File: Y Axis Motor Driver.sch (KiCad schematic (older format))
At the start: 35 parts, among them J1 Motor Y, U1 TMC2209-LA

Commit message: Dodano brakujący footprint dla R1
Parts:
- R1: footprint (none) -> Resistor_SMD:R_0603_1608Metric
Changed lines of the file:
@@
 F 0 "R1" V 1593 1250 50  0000 C CNN
 F 1 "0Ω" V 1684 1250 50  0000 C CNN
-F 2 "" V 1730 1250 50  0001 C CNN
+F 2 "Resistor_SMD:R_0603_1608Metric" V 1730 1250 50  0001 C CNN
 F 3 "~" H 1800 1250 50  0001 C CNN
 	1    1800 1250

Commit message: Routing emergnency, photo barier, relay, voltage detect, analog, footprint improvment
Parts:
- U1: footprint footprints:TMC2209-LA -> footprints:QFN-28_5X5_3X8_EPAD
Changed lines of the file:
@@
 F 0 "U1" H 2850 4850 60  0000 L CNN
 F 1 "TMC2209-LA" H 2850 4750 60  0000 L CNN
-F 2 "footprints:TMC2209-LA" V 3700 3750 60  0001 C CNN
+F 2 "footprints:QFN-28_5X5_3X8_EPAD" V 3700 3750 60  0001 C CNN
 F 3 "https://www.trinamic.com/fileadmin/assets/Products/ICs_Documents/TMC2209_Datasheet_V103.pdf" H 2700 4400 60  0001 C CNN
 F 4 "10.30" H 3750 3750 50  0001 C CNN "Cena"

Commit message: Start TMC routing
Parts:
- removed TP1: Z_OB2, TestPoint:TestPoint_Pad_D1.5mm, symbol Connector:TestPoint
- removed TP2: Z_OB1, TestPoint:TestPoint_Pad_D1.5mm, symbol Connector:TestPoint
- removed TP3: Z_OA2, TestPoint:TestPoint_Pad_D1.5mm, symbol Connector:TestPoint
- removed TP4: Z_OA1, TestPoint:TestPoint_Pad_D1.5mm, symbol Connector:TestPoint
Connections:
- net at U1.1 (OB2): now also FB1.2; no longer FB4.2
- net at U1.21 (OA2): now also FB4.2; no longer FB2.2
- net at U1.24 (OA1): now also FB3.2; no longer FB1.2
- net at U1.26 (OB1): now also FB2.2; no longer FB3.2
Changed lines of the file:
@@
 	0    1    1    0
 $EndComp
-Wire Wire Line
-	4600 3700 6250 3700
-Wire Wire Line
-	6250 3700 6250 3200
-Wire Wire Line
-	4600 3600 6150 3600
-Wire Wire Line
-	6150 3600 6150 3050
 $Comp
 L Device:C_Small C?
@@
 $EndComp
 Wire Wire Line
-	9400 3050 9400 3450
-Wire Wire Line
-	9050 3200 9050 3450
-Wire Wire Line
 	8350 3900 8350 4250
 Connection ~ 8700 3750
@@
 Text Notes 10350 3000 0    50   ~ 0
 Złącze JST XH2.5
-Wire Wire Line
-	8350 3900 8350 3450
-$Comp
-L Connector:TestPoint TP?
-U 1 1 5E249152
-P 8350 3450
-AR Path="/5DE588DC/5E249152" Ref="TP?"  Part="1"
-AR Path="/5DE587B9/5E249152" Ref="TP1"  Part="1"
-F 0 "TP1" V 8250 3500 50  0000 L CNN
-F 1 "Z_OB2" V 8450 3500 50  0000 L CNN
-F 2 "TestPoint:TestPoint_Pad_D1.5mm" H 8550 3450 50  0001 C CNN
-F 3 "~" H 8550 3450 50  0001 C CNN
-	1    8350 3450
-	0    1    1    0
-$EndComp
-$Comp
-L Connector:TestPoint TP?
-U 1 1 5E24915B
-P 8700 3450
-AR Path="/5DE588DC/5E24915B" Ref="TP?"  Part="1"
-AR Path="/5DE587B9/5E24915B" Ref="TP2"  Part="1"
-F 0 "TP2" V 8600 3500 50  0000 L CNN
-F 1 "Z_OB1" V 8800 3500 50  0000 L CNN
-F 2 "TestPoint:TestPoint_Pad_D1.5mm" H 8900 3450 50  0001 C CNN
-F 3 "~" H 8900 3450 50  0001 C CNN
-	1    8700 3450
-	0    1    1    0
-$EndComp
-Wire Wire Line
-	8700 3450 8700 3750
-$Comp
-L Connector:TestPoint TP?
-U 1 1 5E249163
-P 9050 3450
-AR Path="/5DE588DC/5E249163" Ref="TP?"  Part="1"
-AR Path="/5DE587B9/5E249163" Ref="TP3"  Part="1"
-F 0 "TP3" V 8950 3500 50  0000 L CNN
-F 1 "Z_OA2" V 9150 3500 50  0000 L CNN
-F 2 "TestPoint:TestPoint_Pad_D1.5mm" H 9250 3450 50  0001 C CNN
-F 3 "~" H 9250 3450 50  0001 C CNN
-	1    9050 3450
-	0    1    1    0
-$EndComp
-$Comp
-L Connector:TestPoint TP?
-U 1 1 5E24916B
-P 9400 3450
-AR Path="/5DE588DC/5E24916B" Ref="TP?"  Part="1"
-AR Path="/5DE587B9/5E24916B" Ref="TP4"  Part="1"
-F 0 "TP4" V 9300 3500 50  0000 L CNN
-F 1 "Z_OA1" V 9500 3500 50  0000 L CNN
-F 2 "TestPoint:TestPoint_Pad_D1.5mm" H 9600 3450 50  0001 C CNN
-F 3 "~" H 9600 3450 50  0001 C CNN
-	1    9400 3450
-	0    1    1    0
-$EndComp
 Text GLabel 1600 3000 0    50   Input ~ 0
 Y_STEP
@@
 	2900 3100 1600 3100
 Wire Wire Line
-	6350 3800 6350 3750
-Wire Wire Line
-	4600 3800 6350 3800
-Wire Wire Line
 	7250 3050 7500 3050
 Wire Wire Line
@@
 Wire Wire Line
 	7900 3200 9050 3200
-Wire Wire Line
-	6350 3750 7050 3750
-Wire Wire Line
-	4600 3900 7050 3900
 Wire Wire Line
 	6250 3200 7050 3200
@@
 	0    1    1    0
 $EndComp
-Connection ~ 9400 3450
-Connection ~ 9050 3450
 Wire Wire Line
 	7900 3750 8700 3750
@@
 	0    1    1    0
 $EndComp
-Wire Wire Line
-	9400 3450 9400 4250
 $Comp
 L Device:D_TVS_ALT D3
@@
 	8250 4200 9700 4200
 Wire Wire Line
-	9050 3450 9050 4250
-Wire Wire Line
 	9400 4550 9400 5150
 $Comp
@@
 Wire Wire Line
 	9750 3750 9850 3750
+Wire Wire Line
+	6450 3750 7050 3750
+Wire Wire Line
+	4600 3900 6150 3900
+Wire Wire Line
+	6150 3050 6150 3900
+Wire Wire Line
+	6250 3800 4600 3800
+Wire Wire Line
+	6250 3200 6250 3800
+Wire Wire Line
+	4600 3600 6450 3600
+Wire Wire Line
+	6450 3600 6450 3750
+Wire Wire Line
+	7050 3900 6350 3900
+Wire Wire Line
+	6350 3900 6350 3700
+Wire Wire Line
+	6350 3700 4600 3700
+Wire Wire Line
+	9050 3200 9050 4250
+Wire Wire Line
+	9400 3050 9400 4250
 $EndSCHEMATC

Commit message: TMC2209 routing step 2/3
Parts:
- removed C1: 330uF, Capacitor_THT:CP_Radial_D10.0mm_P5.00mm, symbol Device:CP_Small
- removed C2: 10uF, Capacitor_SMD:C_1210_3225Metric, symbol Device:C_Small
- removed C3: 1uF, Capacitor_SMD:C_0805_2012Metric, symbol Device:C_Small
- added C2, C3: 120uF, Capacitor_THT:CP_Radial_D8.0mm_P3.50mm, symbol Device:CP_Small
- added C87: 10uF, Capacitor_SMD:C_1210_3225Metric, symbol Device:C_Small
- added C88: 1uF, Capacitor_SMD:C_0805_2012Metric, symbol Device:C_Small
- added C89: 0.1uF, Capacitor_SMD:C_0603_1608Metric, symbol Device:C_Small
- C4: value 0.1uF -> 10uF; footprint Capacitor_SMD:C_0603_1608Metric -> Capacitor_SMD:C_1210_3225Metric; Cena 0.05982 -> 1.45250; Model CL10B104KB8NNNC -> CL32B106KBJNNNE
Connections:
- net GND: now also C2.2, C3.2, C87.2, C88.2, C89.2; no longer R3.1
- net VCC: now also R3.1
- net VS: now also C2.1, C3.1, C87.1, C88.1, C89.1

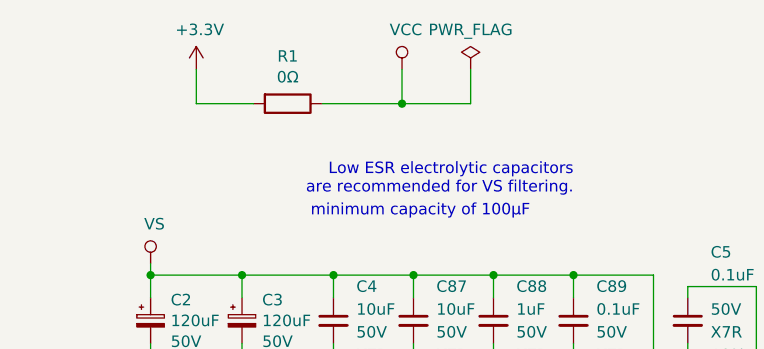
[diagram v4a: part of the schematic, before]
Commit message: Test points, start power plane routing, little change on schematic
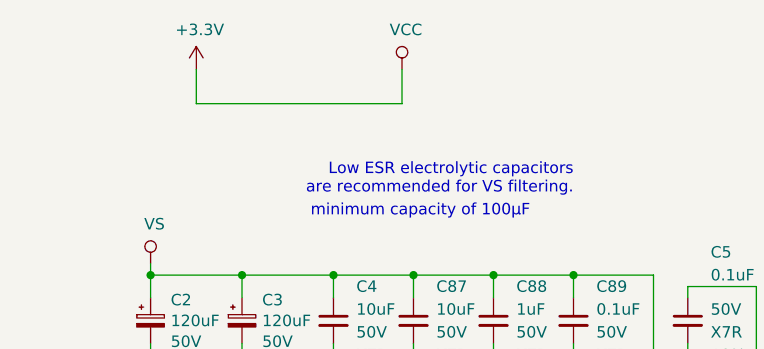
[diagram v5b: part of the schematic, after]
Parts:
- removed R1: 0Ω, Resistor_SMD:R_0603_1608Metric, symbol Device:R
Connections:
- net VCC is gone; now on net +3V3: C6.1, R3.1, U1.15 (VCC_IO), U1.9 (MS1/AD0)
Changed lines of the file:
@@
 	1400 1100 1400 1250
-Wire Wire Line
-	1400 1250 1650 1250
-Wire Wire Line
-	1950 1250 2300 1250
 Wire Wire Line
 	2300 1250 2300 1100
@@
 $EndComp
 $Comp
-L Device:R R?
-U 1 1 5E2371E0
-P 1800 1250
-AR Path="/5DFB2EC0/5E2371E0" Ref="R?"  Part="1"
-AR Path="/5DE587B9/5E2371E0" Ref="R1"  Part="1"
-F 0 "R1" V 1593 1250 50  0000 C CNN
-F 1 "0Ω" V 1684 1250 50  0000 C CNN
-F 2 "Resistor_SMD:R_0603_1608Metric" V 1730 1250 50  0001 C CNN
-F 3 "~" H 1800 1250 50  0001 C CNN
-	1    1800 1250
-	0    1    1    0
-$EndComp
-$Comp
 L Device:D_TVS_ALT D1
 U 1 1 5E251EB1
@@
 Wire Wire Line
 	2200 4800 2200 4850
-$Comp
-L power:PWR_FLAG #FLG0101
-U 1 1 5E3F672C
-P 2600 1100
-F 0 "#FLG0101" H 2600 1175 50  0001 C CNN
-F 1 "PWR_FLAG" H 2600 1273 50  0000 C CNN
-F 2 "" H 2600 1100 50  0001 C CNN
-F 3 "~" H 2600 1100 50  0001 C CNN
-	1    2600 1100
-	1    0    0    -1
-$EndComp
-Wire Wire Line
-	2300 1250 2600 1250
-Wire Wire Line
-	2600 1250 2600 1100
-Connection ~ 2300 1250
+Wire Wire Line
+	1400 1250 2300 1250
 $EndSCHEMATC

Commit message: Added 3d packages, improved TMC2209 footprint
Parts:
- U1: footprint footprints:QFN-28_5X5_3X8_EPAD -> footprints:QFN-28_5X5mm_P0.5mm_EP3.35x.3.35mm
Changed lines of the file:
@@
 F 0 "U1" H 2850 4850 60  0000 L CNN
 F 1 "TMC2209-LA" H 2850 4750 60  0000 L CNN
-F 2 "footprints:QFN-28_5X5_3X8_EPAD" V 3700 3750 60  0001 C CNN
+F 2 "footprints:QFN-28_5X5mm_P0.5mm_EP3.35x.3.35mm" V 3700 3750 60  0001 C CNN
 F 3 "https://www.trinamic.com/fileadmin/assets/Products/ICs_Documents/TMC2209_Datasheet_V103.pdf" H 2700 4400 60  0001 C CNN
 F 4 "10.30" H 3750 3750 50  0001 C CNN "Cena"

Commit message: Updated BOM on schematics
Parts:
- C10, C5, C6, C8, C89: Cena 0.05982 -> 0.07894; Link (none) -> https://www.tme.eu/pl/details/cl10b104kb8nnnc/kondensatory-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; Model CL10B104KB8NNNC -> CL10B104KB8NNNC; Opis (none) -> Kondensator: ceramiczny; MLCC; 100nF; 50V; X7R; ±10%; SMD; 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
- C11, C12, C13, C14: Opis (none) -> Kondensator: ceramiczny; MLCC; 470pF; 100VDC; C0G; ±5%; SMD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
- C4, C87: Link (none) -> https://www.tme.eu/pl/details/cl32b106kbjnnne/kondensatory-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; Opis (none) -> Kondensator: ceramiczny; MLCC; 10uF; 50V; X7R; ±10%; SMD; 1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
- C7: Opis (none) -> Kondensator: ceramiczny; MLCC; 22nF; 50V; X7R; ±10%; SMD; 0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
- C88: Link (none) -> https://www.tme.eu/pl/details/cl21b105kbfnnng/kondensatory-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; Opis (none) -> Kondensator: ceramiczny; MLCC; 1uF; 50V; X7R; ±10%; SMD; 08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
- C9: Opis (none) -> Kondensator: ceramiczny; MLCC; 2,2uF; 10V; X5R; ±10%; SMD; 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
- R3: Link (none) -> https://www.tme.eu/pl/details/smd0603-100k-1%25/rezystory-s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; Model (none) -> 0603SAF1003T5E; Opis (none) -> Rezystor: thick film; SMD; 0603; 100kΩ; 0,1W; ±1%; -55÷155°C; Producent (none) -> ROYAL OHM
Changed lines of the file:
@@
 F 10 "10%" H 5050 3200 50  0001 C CNN "Tolerancja"
 F 11 "SMD" H 5050 3200 50  0001 C CNN "Typ"
+F 12 "Kondensator: ceramiczny; MLCC; 22nF; 50V; X7R; ±10%; SMD; 0603" H 5050 3200 50  0001 C CNN "Opis"
 	1    5050 3200
 	1    0    0    -1
@@
 F 5 "X7R" H 3650 2150 50  0000 L CNN "Dielektryk"
 F 6 "10%" H 3650 2050 50  0000 L CNN "Tolerancja"
-F 7 "CL10B104KB8NNNC " H 3550 2200 50  0001 C CNN "Model"
-F 8 "0.05982" H 3550 2200 50  0001 C CNN "Cena"
+F 7 "CL10B104KB8NNNC" H 3550 2200 50  0001 C CNN "Model"
+F 8 "0.07894" H 3550 2200 50  0001 C CNN "Cena"
 F 9 "SAMSUNG" H 3550 2200 50  0001 C CNN "Producent"
 F 10 "SMD" H 3550 2200 50  0001 C CNN "Typ"
+F 11 "https://www.tme.eu/pl/details/cl10b104kb8nnnc/kondensatory-mlcc-smd-0603/samsung/" H 3550 2200 50  0001 C CNN "Link"
+F 12 "Kondensator: ceramiczny; MLCC; 100nF; 50V; X7R; ±10%; SMD; 0603" H 3550 2200 50  0001 C CNN "Opis"
 	1    3550 2200
 	1    0    0    -1
@@
 F 5 "X7R" H 4250 2150 50  0000 L CNN "Dielektryk"
 F 6 "10%" H 4250 2050 50  0000 L CNN "Tolerancja"
-F 7 "CL10B104KB8NNNC " H 4150 2200 50  0001 C CNN "Model"
-F 8 "0.05982" H 4150 2200 50  0001 C CNN "Cena"
+F 7 "CL10B104KB8NNNC" H 4150 2200 50  0001 C CNN "Model"
+F 8 "0.07894" H 4150 2200 50  0001 C CNN "Cena"
 F 9 "SAMSUNG" H 4150 2200 50  0001 C CNN "Producent"
 F 10 "SMD" H 4150 2200 50  0001 C CNN "Typ"
+F 11 "https://www.tme.eu/pl/details/cl10b104kb8nnnc/kondensatory-mlcc-smd-0603/samsung/" H 4150 2200 50  0001 C CNN "Link"
+F 12 "Kondensator: ceramiczny; MLCC; 100nF; 50V; X7R; ±10%; SMD; 0603" H 4150 2200 50  0001 C CNN "Opis"
 	1    4150 2200
 	1    0    0    -1
@@
 F 5 "X7R" H 5492 4359 50  0000 L CNN "Dielektryk"
 F 6 "10%" H 5492 4268 50  0000 L CNN "Tolerancja"
-F 7 "CL10B104KB8NNNC " H 5400 4450 50  0001 C CNN "Model"
-F 8 "0.05982" H 5400 4450 50  0001 C CNN "Cena"
+F 7 "CL10B104KB8NNNC" H 5400 4450 50  0001 C CNN "Model"
+F 8 "0.07894" H 5400 4450 50  0001 C CNN "Cena"
 F 9 "SAMSUNG" H 5400 4450 50  0001 C CNN "Producent"
 F 10 "SMD" H 5400 4450 50  0001 C CNN "Typ"
+F 11 "https://www.tme.eu/pl/details/cl10b104kb8nnnc/kondensatory-mlcc-smd-0603/samsung/" H 5400 4450 50  0001 C CNN "Link"
+F 12 "Kondensator: ceramiczny; MLCC; 100nF; 50V; X7R; ±10%; SMD; 0603" H 5400 4450 50  0001 C CNN "Opis"
 	1    5400 4450
 	1    0    0    -1
@@
 F 5 "X7R" H 6542 4359 50  0000 L CNN "Dielektryk"
 F 6 "10%" H 6542 4268 50  0000 L CNN "Tolerancja"
-F 7 "CL10B104KB8NNNC " H 6450 4450 50  0001 C CNN "Model"
-F 8 "0.05982" H 6450 4450 50  0001 C CNN "Cena"
+F 7 "CL10B104KB8NNNC" H 6450 4450 50  0001 C CNN "Model"
+F 8 "0.07894" H 6450 4450 50  0001 C CNN "Cena"
 F 9 "SAMSUNG" H 6450 4450 50  0001 C CNN "Producent"
 F 10 "SMD" H 6450 4450 50  0001 C CNN "Typ"
+F 11 "https://www.tme.eu/pl/details/cl10b104kb8nnnc/kondensatory-mlcc-smd-0603/samsung/" H 6450 4450 50  0001 C CNN "Link"
+F 12 "Kondensator: ceramiczny; MLCC; 100nF; 50V; X7R; ±10%; SMD; 0603" H 6450 4450 50  0001 C CNN "Opis"
 	1    6450 4450
 	1    0    0    -1
@@
 F 10 "KEMET" H 7900 4400 50  0001 C CNN "Producent"
 F 11 "SMD" H 7900 4400 50  0001 C CNN "Typ"
+F 12 "Kondensator: ceramiczny; MLCC; 470pF; 100VDC; C0G; ±5%; SMD; 0805" H 7900 4400 50  0001 C CNN "Opis"
 	1    7900 4400
 	1    0    0    -1
@@
 F 10 "KEMET" H 7500 2650 50  0001 C CNN "Producent"
 F 11 "SMD" H 7500 2650 50  0001 C CNN "Typ"
+F 12 "Kondensator: ceramiczny; MLCC; 470pF; 100VDC; C0G; ±5%; SMD; 0805" H 7500 2650 50  0001 C CNN "Opis"
 	1    7500 2650
 	1    0    0    -1
@@
 F 10 "KEMET" H 7500 4400 50  0001 C CNN "Producent"
 F 11 "SMD" H 7500 4400 50  0001 C CNN "Typ"
+F 12 "Kondensator: ceramiczny; MLCC; 470pF; 100VDC; C0G; ±5%; SMD; 0805" H 7500 4400 50  0001 C CNN "Opis"
 	1    7500 4400
 	1    0    0    -1
@@
 F 10 "KEMET" H 7900 2650 50  0001 C CNN "Producent"
 F 11 "SMD" H 7900 2650 50  0001 C CNN "Typ"
+F 12 "Kondensator: ceramiczny; MLCC; 470pF; 100VDC; C0G; ±5%; SMD; 0805" H 7900 2650 50  0001 C CNN "Opis"
 	1    7900 2650
 	1    0    0    -1
@@
 F 9 "SAMSUNG" H 5450 3200 50  0001 C CNN "Producent"
 F 10 "SMD" H 5450 3200 50  0001 C CNN "Typ"
+F 11 "Kondensator: ceramiczny; MLCC; 2,2uF; 10V; X5R; ±10%; SMD; 0603" H 5450 3200 50  0001 C CNN "Opis"
 	1    5450 3200
 	1    0    0    -1
@@
 F 9 "10%" H 2000 2200 50  0001 C CNN "Tolerancja"
 F 10 "SMD" H 2000 2200 50  0001 C CNN "Typ"
+F 11 "https://www.tme.eu/pl/details/cl32b106kbjnnne/kondensatory-mlcc-smd-1210/samsung/" H 2000 2200 50  0001 C CNN "Link"
+F 12 "Kondensator: ceramiczny; MLCC; 10uF; 50V; X7R; ±10%; SMD; 1210" H 2000 2200 50  0001 C CNN "Opis"
 	1    2000 2200
 	1    0    0    -1
@@
 F 4 "50V" H 3150 2150 50  0000 L CNN "Napięcie"
 F 5 "X7R" H 3150 2050 50  0000 L CNN "Dielektryk"
-F 6 "0.05982" H 3050 2200 50  0001 C CNN "Cena"
-F 7 "CL10B104KB8NNNC " H 3050 2200 50  0001 C CNN "Model"
+F 6 "0.07894" H 3050 2200 50  0001 C CNN "Cena"
+F 7 "CL10B104KB8NNNC" H 3050 2200 50  0001 C CNN "Model"
 F 8 "SAMSUNG" H 3050 2200 50  0001 C CNN "Producent"
 F 9 "10%" H 3050 2200 50  0001 C CNN "Tolerancja"
 F 10 "SMD" H 3050 2200 50  0001 C CNN "Typ"
+F 11 "https://www.tme.eu/pl/details/cl10b104kb8nnnc/kondensatory-mlcc-smd-0603/samsung/" H 3050 2200 50  0001 C CNN "Link"
+F 12 "Kondensator: ceramiczny; MLCC; 100nF; 50V; X7R; ±10%; SMD; 0603" H 3050 2200 50  0001 C CNN "Opis"
 	1    3050 2200
 	1    0    0    -1
@@
 F 9 "10%" H 2700 2200 50  0001 C CNN "Tolerancja"
 F 10 "SMD" H 2700 2200 50  0001 C CNN "Typ"
+F 11 "https://www.tme.eu/pl/details/cl21b105kbfnnng/kondensatory-mlcc-smd-0805/samsung/" H 2700 2200 50  0001 C CNN "Link"
+F 12 "Kondensator: ceramiczny; MLCC; 1uF; 50V; X7R; ±10%; SMD; 0805" H 2700 2200 50  0001 C CNN "Opis"
 	1    2700 2200
 	1    0    0    -1
@@
 F 9 "10%" H 2350 2200 50  0001 C CNN "Tolerancja"
 F 10 "SMD" H 2350 2200 50  0001 C CNN "Typ"
+F 11 "https://www.tme.eu/pl/details/cl32b106kbjnnne/kondensatory-mlcc-smd-1210/samsung/" H 2350 2200 50  0001 C CNN "Link"
+F 12 "Kondensator: ceramiczny; MLCC; 10uF; 50V; X7R; ±10%; SMD; 1210" H 2350 2200 50  0001 C CNN "Opis"
 	1    2350 2200
 	1    0    0    -1
@@
 F 2 "Resistor_SMD:R_0603_1608Metric" V 2330 4700 50  0001 C CNN
 F 3 "~" H 2400 4700 50  0001 C CNN
-F 4 "" H 2400 4700 50  0001 C CNN "Model"
+F 4 "0603SAF1003T5E" H 2400 4700 50  0001 C CNN "Model"
 F 5 "0.04651" H 2400 4700 50  0001 C CNN "Cena"
 F 6 "SMD" H 2400 4700 50  0001 C CNN "Typ"
+F 7 "https://www.tme.eu/pl/details/smd0603-100k-1%25/rezystory-smd-0603/royal-ohm/0603saf1003t5e/" H 2400 4700 50  0001 C CNN "Link"
+F 8 "Rezystor: thick film; SMD; 0603; 100kΩ; 0,1W; ±1%; -55÷155°C" H 2400 4700 50  0001 C CNN "Opis"
+F 9 "ROYAL OHM" H 2400 4700 50  0001 C CNN "Producent"
 	1    2400 4700
 	-1   0    0    1
